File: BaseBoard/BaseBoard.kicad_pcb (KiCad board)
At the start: 4 copper layers, 50 x 35 mm, 59 parts, among them J1 locked, J2 Serial Port, J3 base connector, Q1 PMN48XP, Q2 SSM6L820R, SW1 Battery switch, SW2 boot, SW3 Reset, U1 ESP32-WROOM-E, U3 MCP73831-2ACI-OT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

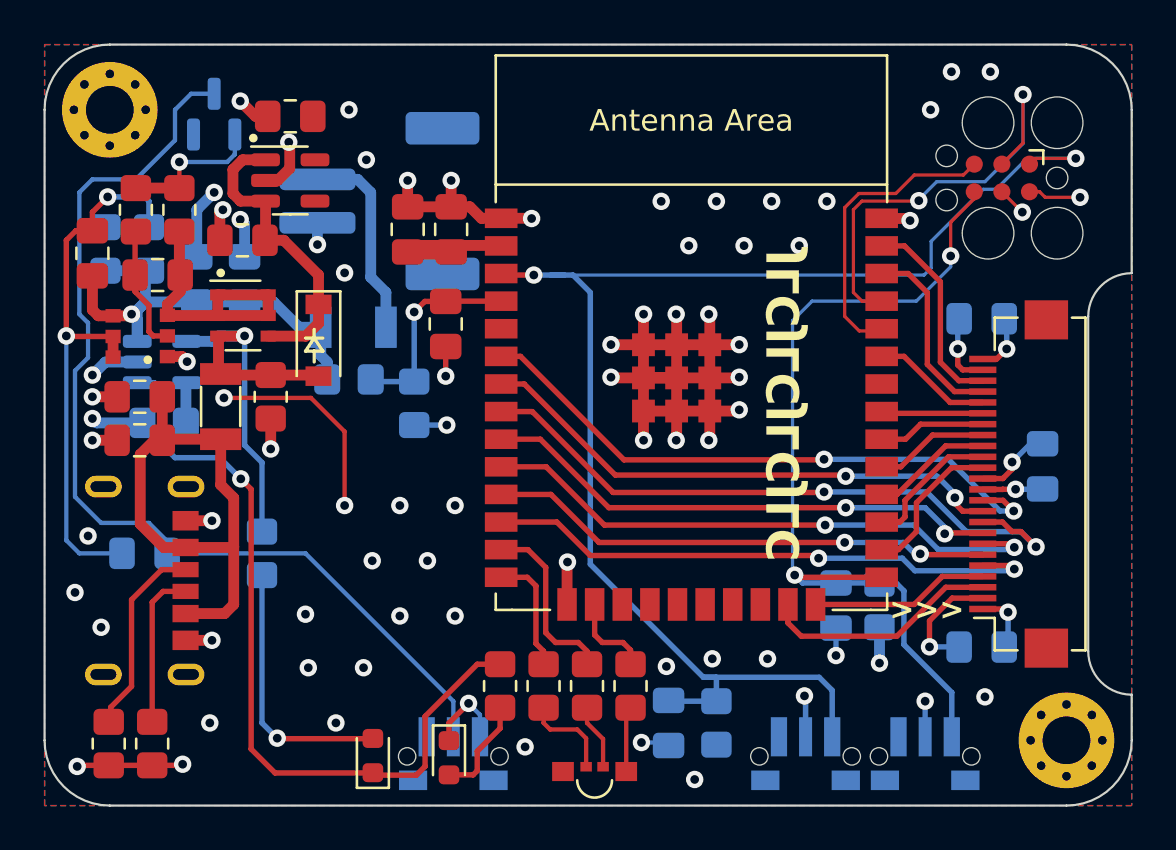
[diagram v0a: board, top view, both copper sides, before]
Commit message: Reorganizes some traces on the BaseBoard
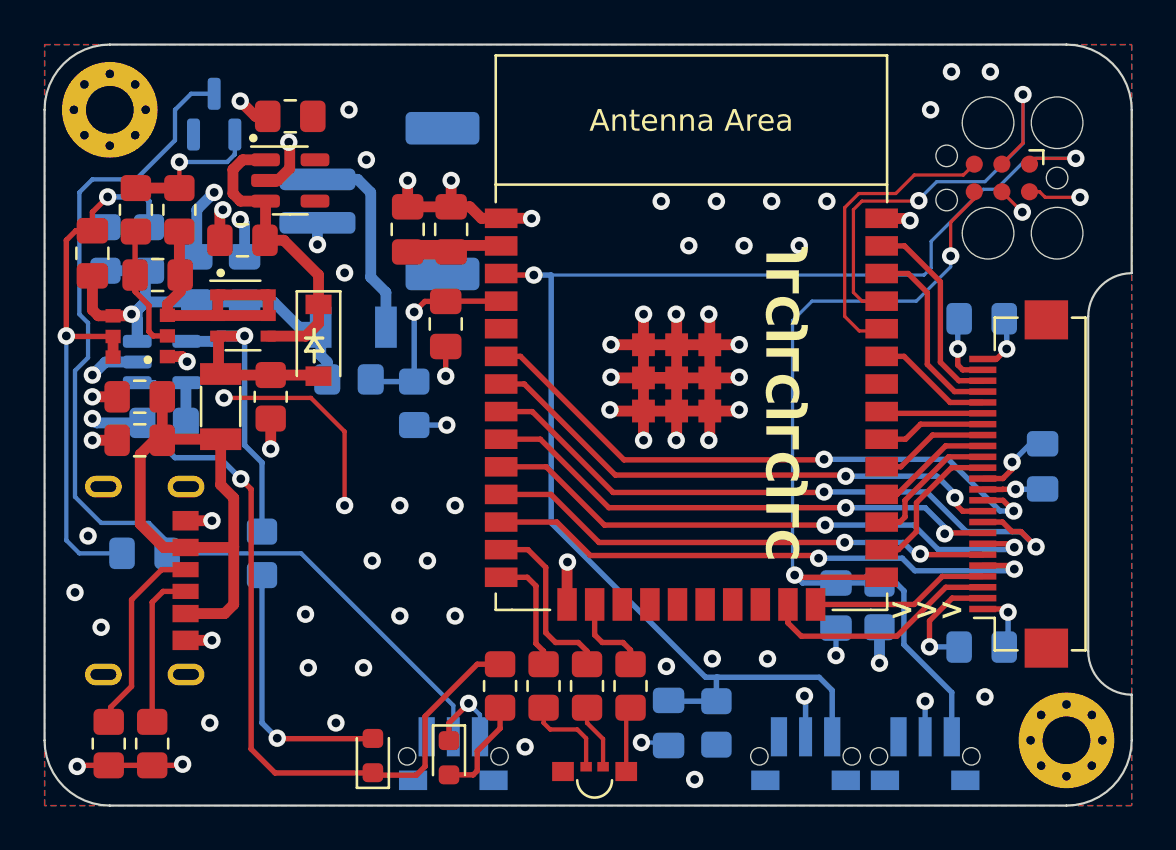
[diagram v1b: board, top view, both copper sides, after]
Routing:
- net ESP_EN: track 66.4 -> 64.7 mm
- net GND: track 100.8 -> 102.3 mm, vias 43 -> 44
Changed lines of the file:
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@@
         (effects (font (size 1 1) (thickness 0.15)))
     )
-    (fp_text value "LED green" (at 0 1.43 90) (layer "F.Fab")
+    (fp_text value "LED green" (at 0 1.43 90) (layer "F.Fab") hide
         (effects (font (size 1 1) (thickness 0.15)))
     )
@@
         (effects (font (size 1 1) (thickness 0.15)))
     )
-    (fp_text value "LED red" (at 0 1.43 90) (layer "F.Fab")
+    (fp_text value "LED red" (at 0 1.43 90) (layer "F.Fab") hide
         (effects (font (size 1 1) (thickness 0.15)))
     )
@@
   (segment (start 149.07 93.805) (end 149.07 96.855) (width 0.5) (layer "F.Cu") (net 2))
   (segment (start 122.95 113.15) (end 121.55 113.15) (width 0.25) (layer "F.Cu") (net 2))
+  (segment (start 146 96.8) (end 146.055 96.855) (width 0.5) (layer "F.Cu") (net 2))
   (segment (start 138.6 111.2) (end 139.5 110.3) (width 0.25) (layer "F.Cu") (net 2))
   (segment (start 150.595 96.855) (end 147.545 96.855) (width 0.5) (layer "F.Cu") (net 2))
@@
   (segment (start 122.2 98.2) (end 123.3375 98.2) (width 0.5) (layer "F.Cu") (net 2))
   (segment (start 158.51 88) (end 158.5 87.99) (width 0.5) (layer "F.Cu") (net 2))
+  (segment (start 146.055 96.855) (end 147.545 96.855) (width 0.5) (layer "F.Cu") (net 2))
   (segment (start 130.1625 86.25) (end 130.722849 86.25) (width 0.5) (layer "F.Cu") (net 2))
   (segment (start 164.074022 99.96) (end 163.15 99.96) (width 0.25) (layer "F.Cu") (net 2))
@@
   (via (at 164.25 94) (size 0.8) (drill 0.4) (layers "F.Cu" "B.Cu") (net 2))
   (via (at 144.05 103.8) (size 0.8) (drill 0.4) (layers "F.Cu" "B.Cu") (net 2))
+  (via (at 146 96.8) (size 0.8) (drill 0.4) (layers "F.Cu" "B.Cu") (net 2))
   (segment (start 137 97.5) (end 138.5 97.5) (width 0.25) (layer "B.Cu") (net 2))
   (segment (start 127 87.6) (end 127 89.7625) (width 0.5) (layer "B.Cu") (net 2))
@@
   (via (at 167.428848 85.235) (size 0.8) (drill 0.4) (layers "F.Cu" "B.Cu") (net 5))
   (via (at 142.5 90.6) (size 0.8) (drill 0.4) (layers "F.Cu" "B.Cu") (net 5))
-  (segment (start 145.1 103.9) (end 145.1 91.4) (width 0.25) (layer "B.Cu") (net 5))
+  (segment (start 143.3 102) (end 143.3 90.6) (width 0.25) (layer "B.Cu") (net 5))
+  (segment (start 151 109.1) (end 150.4 109.1) (width 0.25) (layer "B.Cu") (net 5))
   (segment (start 163.768552 86.655699) (end 165.189251 85.235) (width 0.15) (layer "B.Cu") (net 5))
   (segment (start 160.449251 90.6) (end 160.775 90.274251) (width 0.15) (layer "B.Cu") (net 5))
   (segment (start 143.3 90.6) (end 160.449251 90.6) (width 0.15) (layer "B.Cu") (net 5))
   (segment (start 160.775 89.049251) (end 163.168552 86.655699) (width 0.15) (layer "B.Cu") (net 5))
-  (segment (start 150.3 109.1) (end 150.9 109.1) (width 0.25) (layer "B.Cu") (net 5))
-  (segment (start 156.225 111.8375) (end 156.225 109.7) (width 0.25) (layer "B.Cu") (net 5))
-  (segment (start 143.9 90.6) (end 142.5 90.6) (width 0.25) (layer "B.Cu") (net 5))
   (segment (start 148.7375 110.2) (end 148.7 110.1625) (width 0.25) (layer "B.Cu") (net 5))
+  (segment (start 156.225 111.8375) (end 156.225 109.7) (width 0.25) (layer "B.Cu") (net 5))
   (segment (start 165.189251 85.235) (end 167.428848 85.235) (width 0.15) (layer "B.Cu") (net 5))
+  (segment (start 150.4 109.1) (end 143.3 102) (width 0.25) (layer "B.Cu") (net 5))
   (segment (start 150.9 109.1) (end 150.9 110.2) (width 0.25) (layer "B.Cu") (net 5))
-  (segment (start 156.225 109.7) (end 155.625 109.1) (width 0.25) (layer "B.Cu") (net 5))
-  (segment (start 145.1 91.4) (end 144.3 90.6) (width 0.25) (layer "B.Cu") (net 5))
+  (segment (start 142.5 90.6) (end 143.3 90.6) (width 0.25) (layer "B.Cu") (net 5))
   (segment (start 163.168552 86.655699) (end 163.768552 86.655699) (width 0.15) (layer "B.Cu") (net 5))
   (segment (start 160.775 90.274251) (end 160.775 89.049251) (width 0.15) (layer "B.Cu") (net 5))
+  (segment (start 156.225 109.7) (end 155.625 109.1) (width 0.25) (layer "B.Cu") (net 5))
   (segment (start 150.9 110.2) (end 148.7375 110.2) (width 0.25) (layer "B.Cu") (net 5))
-  (segment (start 155.625 109.1) (end 150.3 109.1) (width 0.25) (layer "B.Cu") (net 5))
-  (segment (start 150.3 109.1) (end 145.1 103.9) (width 0.25) (layer "B.Cu") (net 5))
-  (segment (start 144.3 90.6) (end 143.3 90.6) (width 0.25) (layer "B.Cu") (net 5))
+  (segment (start 155.625 109.1) (end 150.9 109.1) (width 0.25) (layer "B.Cu") (net 5))
   (segment (start 137 92.3) (end 137.4875 91.8125) (width 0.25) (layer "F.Cu") (net 6))
   (segment (start 138.45 91.8125) (end 138.4625 91.8) (width 0.25) (layer "F.Cu") (net 6))
@@
   (segment (start 130.7 111.9) (end 130 111.2) (width 0.25) (layer "B.Cu") (net 49))
   (segment (start 121.6 86.8) (end 122.2 86.2) (width 0.2) (layer "B.Cu") (net 50))
-  (segment (start 138.8 111.8375) (end 138.8 110.2) (width 0.2) (layer "B.Cu") (net 50))
   (segment (start 121.6 88.4) (end 121.6 92.4) (width 0.2) (layer "B.Cu") (net 50))
+  (segment (start 138.8 111.8375) (end 138.8 110.4) (width 0.2) (layer "B.Cu") (net 50))
+  (segment (start 131.8 103.4) (end 125.6375 103.4) (width 0.2) (layer "B.Cu") (net 50))
   (segment (start 122.2 86.2) (end 124.2 86.2) (width 0.2) (layer "B.Cu") (net 50))
-  (segment (start 132 103.4) (end 125.6375 103.4) (width 0.2) (layer "B.Cu") (net 50))
-  (segment (start 138.8 110.2) (end 132 103.4) (width 0.2) (layer "B.Cu") (net 50))
   (segment (start 121.6 88.4) (end 121.6 86.8) (width 0.2) (layer "B.Cu") (net 50))
   (segment (start 124.8 102) (end 125.6375 102.8375) (width 0.2) (layer "B.Cu") (net 50))
@@
   (segment (start 122.8 88.4) (end 121.6 88.4) (width 0.2) (layer "B.Cu") (net 50))
   (segment (start 122.6 102) (end 124.8 102) (width 0.2) (layer "B.Cu") (net 50))
+  (segment (start 138.8 110.4) (end 131.8 103.4) (width 0.2) (layer "B.Cu") (net 50))
   (segment (start 126 83) (end 126.7375 82.2625) (width 0.2) (layer "B.Cu") (net 50))
   (segment (start 126 84.4) (end 126 83) (width 0.2) (layer "B.Cu") (net 50))

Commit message: Adds label for on/off button
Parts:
- added kibuzzard-63029C06: G***, kibuzzard-63029C06, B.Cu at (138.8, 109.8)
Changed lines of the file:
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@@
-(kicad_pcb (version 20220331) (generator pcbnew)
+(kicad_pcb (version 20220818) (generator pcbnew)
   (general
     (thickness 1.6)
@@
       (connect_pads (clearance 0))
       (min_thickness 0.254) (filled_areas_thickness no)
-      (keepout (tracks allowed) (vias not_allowed) (pads allowed ) (copperpour not_allowed) (footprints not_allowed))
+      (keepout (tracks allowed) (vias not_allowed) (pads allowed) (copperpour not_allowed) (footprints not_allowed))
       (fill (thermal_gap 0.508) (thermal_bridge_width 0.508))
       (polygon
@@
       (thermal_bridge_angle 45))
   )
+  (footprint "kibuzzard-63029C06" (layer "B.Cu")
+    (at 138.8 109.75 180)
+    (descr "Generated with KiBuzzard")
+    (tags "kb_params=eyJBbGlnbm1lbnRDaG9pY2UiOiAiQ2VudGVyIiwgIkNhcExlZnRDaG9pY2UiOiAiWyIsICJDYXBSaWdodENob2ljZSI6ICJdIiwgIkZvbnRDb21ib0JveCI6ICJVYnVudHVNb25vLUIiLCAiSGVpZ2h0Q3RybCI6ICIxIiwgIkxheWVyQ29tYm9Cb3giOiAiRi5TaWxrUyIsICJNdWx0aUxpbmVUZXh0IjogIm9uL29mZiIsICJQYWRkaW5nQm90dG9tQ3RybCI6ICI1IiwgIlBhZGRpbmdMZWZ0Q3RybCI6ICI1IiwgIlBhZGRpbmdSaWdodEN0cmwiOiAiNSIsICJQYWRkaW5nVG9wQ3RybCI6ICI1IiwgIldpZHRoQ3RybCI6ICIifQ==")
+    (attr board_only exclude_from_pos_files exclude_from_bom)
+    (fp_text reference "kibuzzard-63029C06" (at 0 4.064529) (layer "B.SilkS") hide
+        (effects (font (size 0 0)) (justify mirror))
+    )
+    (fp_text value "G***" (at 0 -4.064529) (layer "B.SilkS") hide
+        (effects (font (size 0 0)) (justify mirror))
+    )
+    (fp_poly
+      (pts
+        (xy -2.153444 -0.0508)
+        (xy -2.144514 -0.141288)
+        (xy -2.117725 -0.212725)
+        (xy -2.071092 -0.259159)
+        (xy -2.002631 -0.274638)
+        (xy -1.935758 -0.259159)
+        (xy -1.887537 -0.212725)
+        (xy -1.858367 -0.141288)
+        (xy -1.848644 -0.0508)
+        (xy -1.857573 0.039489)
+        (xy -1.884362 0.110331)
+        (xy -1.930995 0.15617)
+        (xy -1.999456 0.17145)
+        (xy -2.06633 0.15617)
+        (xy -2.11455 0.110331)
+        (xy -2.14372 0.039489)
+        (xy -2.153444 -0.0508)
+      )
+      (stroke (width 0) (type solid)) (fill solid) (layer "B.SilkS"))
+    (fp_poly
+      (pts
+        (xy 0.227806 -0.0508)
+        (xy 0.236736 -0.141288)
+        (xy 0.263525 -0.212725)
+        (xy 0.310158 -0.259159)
+        (xy 0.378619 -0.274638)
+        (xy 0.445492 -0.259159)
+        (xy 0.493713 -0.212725)
+        (xy 0.522883 -0.141288)
+        (xy 0.532606 -0.0508)
+        (xy 0.523677 0.039489)
+        (xy 0.496888 0.110331)
+        (xy 0.450255 0.15617)
+        (xy 0.381794 0.17145)
+        (xy 0.31492 0.15617)
+        (xy 0.2667 0.110331)
+        (xy 0.23753 0.039489)
+        (xy 0.227806 -0.0508)
+      )
+      (stroke (width 0) (type solid)) (fill solid) (layer "B.SilkS"))
+    (fp_poly
+      (pts
+        (xy -2.351881 1.016529)
+        (xy -2.68261 1.016529)
+        (xy -2.68261 -1.016529)
+        (xy -2.351881 -1.016529)
+        (xy -1.999456 -1.016529)
+        (xy -1.999456 -0.4445)
+        (xy -2.075061 -0.437356)
+        (xy -2.143125 -0.415925)
+        (xy -2.203053 -0.381397)
+        (xy -2.25425 -0.334963)
+        (xy -2.295723 -0.277614)
+        (xy -2.326481 -0.210344)
+        (xy -2.345531 -0.133945)
+        (xy -2.351881 -0.049212)
+        (xy -2.345333 0.03433)
+        (xy -2.325688 0.110331)
+        (xy -2.294334 0.177403)
+        (xy -2.252663 0.234156)
+        (xy -2.201267 0.279797)
+        (xy -2.140744 0.313531)
+        (xy -2.072878 0.334367)
+        (xy -1.999456 0.341312)
+        (xy -1.925042 0.334367)
+        (xy -1.857375 0.313531)
+        (xy -1.797447 0.279797)
+        (xy -1.74625 0.234156)
+        (xy -1.704777 0.177403)
+        (xy -1.674019 0.110331)
+        (xy -1.654969 0.03433)
+        (xy -1.648619 -0.049212)
+        (xy -1.654969 -0.133945)
+        (xy -1.674019 -0.210344)
+        (xy -1.704578 -0.277614)
+        (xy -1.745456 -0.334963)
+        (xy -1.796058 -0.381397)
+        (xy -1.855788 -0.415925)
+        (xy -1.923852 -0.437356)
+        (xy -1.999456 -0.4445)
+        (xy -1.999456 -1.016529)
+        (xy -0.904081 -1.016529)
+        (xy -0.904081 -0.423863)
+        (xy -1.099344 -0.423863)
+        (xy -1.099344 -0.028575)
+        (xy -1.105297 0.061516)
+        (xy -1.123156 0.122237)
+        (xy -1.219994 0.168275)
+        (xy -1.26365 0.166687)
+        (xy -1.308894 0.161925)
+        (xy -1.308894 -0.423863)
+        (xy -1.504156 -0.423863)
+        (xy -1.504156 0.29845)
+        (xy -1.445617 0.312341)
+        (xy -1.374775 0.325437)
+        (xy -1.294408 0.334962)
+        (xy -1.207294 0.338137)
+        (xy -1.125934 0.331986)
+        (xy -1.059656 0.313531)
+        (xy -0.966787 0.243681)
+        (xy -0.918369 0.135731)
+        (xy -0.907653 0.069652)
+        (xy -0.904081 -0.003175)
+        (xy -0.904081 -0.423863)
+        (xy -0.904081 -1.016529)
+        (xy -0.532606 -1.016529)
+        (xy -0.532606 -0.6858)
+        (xy -0.735806 -0.6858)
+        (xy -0.291306 0.6858)
+        (xy -0.091281 0.6858)
+        (xy -0.532606 -0.6858)
+        (xy -0.532606 -1.016529)
+        (xy 0.381794 -1.016529)
+        (xy 0.381794 -0.4445)
+        (xy 0.306189 -0.437356)
+        (xy 0.238125 -0.415925)
+        (xy 0.178197 -0.381397)
+        (xy 0.127 -0.334963)
+        (xy 0.085527 -0.277614)
+        (xy 0.054769 -0.210344)
+        (xy 0.035719 -0.133945)
+        (xy 0.029369 -0.049212)
+        (xy 0.035917 0.03433)
+        (xy 0.055563 0.110331)
+        (xy 0.086916 0.177403)
+        (xy 0.128588 0.234156)
+        (xy 0.179983 0.279797)
+        (xy 0.240506 0.313531)
+        (xy 0.308372 0.334367)
+        (xy 0.381794 0.341312)
+        (xy 0.456208 0.334367)
+        (xy 0.523875 0.313531)
+        (xy 0.583803 0.279797)
+        (xy 0.635 0.234156)
+        (xy 0.676473 0.177403)
+        (xy 0.707231 0.110331)
+        (xy 0.726281 0.03433)
+        (xy 0.732631 -0.049212)
+        (xy 0.726281 -0.133945)
+        (xy 0.707231 -0.210344)
+        (xy 0.676672 -0.277614)
+        (xy 0.635794 -0.334963)
+        (xy 0.585192 -0.381397)
+        (xy 0.525463 -0.415925)
+        (xy 0.457398 -0.437356)
+        (xy 0.381794 -0.4445)
+        (xy 0.381794 -1.016529)
+        (xy 0.997744 -1.016529)
+        (xy 0.997744 -0.423863)
+        (xy 0.997744 0.160337)
+        (xy 0.834231 0.160337)
+        (xy 0.834231 0.322262)
+        (xy 0.997744 0.322262)
+        (xy 0.997744 0.365125)
+        (xy 1.004292 0.447873)
+        (xy 1.023938 0.515144)
+        (xy 1.094581 0.610394)
+        (xy 1.196181 0.661194)
+        (xy 1.313656 0.676275)
+        (xy 1.440656 0.665162)
+        (xy 1.558131 0.62865)
+        (xy 1.524794 0.4699)
+        (xy 1.433513 0.496094)
+        (xy 1.329531 0.509588)
+        (xy 1.277938 0.504825)
+        (xy 1.235075 0.484187)
+        (xy 1.205706 0.438944)
+        (xy 1.194594 0.36195)
+        (xy 1.194594 0.322262)
+        (xy 1.500981 0.322262)
+        (xy 1.500981 0.160337)
+        (xy 1.194594 0.160337)
+        (xy 1.194594 -0.423863)
+        (xy 0.997744 -0.423863)
+        (xy 0.997744 -1.016529)
+        (xy 1.791494 -1.016529)
+        (xy 1.791494 -0.423863)
+        (xy 1.791494 0.160337)
+        (xy 1.627981 0.160337)
+        (xy 1.627981 0.322262)
+        (xy 1.791494 0.322262)
+        (xy 1.791494 0.365125)
+        (xy 1.798042 0.447873)
+        (xy 1.817688 0.515144)
+        (xy 1.888331 0.610394)
+        (xy 1.989931 0.661194)
+        (xy 2.107406 0.676275)
+        (xy 2.234406 0.665162)
+        (xy 2.351881 0.62865)
+        (xy 2.318544 0.4699)
+        (xy 2.227263 0.496094)
+        (xy 2.123281 0.509588)
+        (xy 2.071688 0.504825)
+        (xy 2.028825 0.484187)
+        (xy 1.999456 0.438944)
+        (xy 1.988344 0.36195)
+        (xy 1.988344 0.322262)
+        (xy 2.294731 0.322262)
+        (xy 2.294731 0.160337)
+        (xy 1.988344 0.160337)
+        (xy 1.988344 -0.423863)
+        (xy 1.791494 -0.423863)
+        (xy 1.791494 -1.016529)
+        (xy 2.351881 -1.016529)
+        (xy 2.68261 -1.016529)
+        (xy 2.68261 1.016529)
+        (xy 2.351881 1.016529)
+        (xy -2.351881 1.016529)
+      )
+      (stroke (width 0) (type solid)) (fill solid) (layer "B.SilkS"))
+  )
   (footprint "Package_TO_SOT_SMD:SOT-23" (layer "B.Cu")
     (at 127.8 83.2 90)
@@
     (connect_pads (clearance 0))
     (min_thickness 0.254) (filled_areas_thickness no)
-    (keepout (tracks not_allowed) (vias not_allowed) (pads not_allowed ) (copperpour not_allowed) (footprints allowed))
+    (keepout (tracks not_allowed) (vias not_allowed) (pads not_allowed) (copperpour not_allowed) (footprints allowed))
     (fill (thermal_gap 0.508) (thermal_bridge_width 0.508) (island_removal_mode 2) (island_area_min 10))
     (polygon

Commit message: Update version label on PCBs to 1.0
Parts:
- removed kibuzzard-62829F6C: G***, kibuzzard-62829F6C
- added kibuzzard-63029CBF: G***, kibuzzard-63029CBF, B.Cu at (131.6, 113.4)

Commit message: Small adjustment to the height of the on/off label
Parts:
- moved kibuzzard-63029C06 0.15 mm to (138.8, 109.6)
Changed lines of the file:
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@@
     (attr board_only exclude_from_pos_files exclude_from_bom)
     (fp_text reference "kibuzzard-63029CBF" (at 0 3.891492) (layer "B.SilkS") hide
-        (effects (font (size 0 0)) (justify mirror))
+        (effects (font (size 0 0) (thickness 0.15)) (justify mirror))
     )
     (fp_text value "G***" (at 0 -3.891492) (layer "B.SilkS") hide
-        (effects (font (size 0 0)) (justify mirror))
+        (effects (font (size 0 0) (thickness 0.15)) (justify mirror))
     )
     (fp_poly
@@
   )
   (footprint "kibuzzard-63029C06" (layer "B.Cu")
-    (at 138.8 109.75 180)
+    (at 138.8 109.6 180)
     (descr "Generated with KiBuzzard")
     (tags "kb_params=eyJBbGlnbm1lbnRDaG9pY2UiOiAiQ2VudGVyIiwgIkNhcExlZnRDaG9pY2UiOiAiWyIsICJDYXBSaWdodENob2ljZSI6ICJdIiwgIkZvbnRDb21ib0JveCI6ICJVYnVudHVNb25vLUIiLCAiSGVpZ2h0Q3RybCI6ICIxIiwgIkxheWVyQ29tYm9Cb3giOiAiRi5TaWxrUyIsICJNdWx0aUxpbmVUZXh0IjogIm9uL29mZiIsICJQYWRkaW5nQm90dG9tQ3RybCI6ICI1IiwgIlBhZGRpbmdMZWZ0Q3RybCI6ICI1IiwgIlBhZGRpbmdSaWdodEN0cmwiOiAiNSIsICJQYWRkaW5nVG9wQ3RybCI6ICI1IiwgIldpZHRoQ3RybCI6ICIifQ==")
     (attr board_only exclude_from_pos_files exclude_from_bom)
     (fp_text reference "kibuzzard-63029C06" (at 0 4.064529) (layer "B.SilkS") hide
-        (effects (font (size 0 0)) (justify mirror))
+        (effects (font (size 0 0) (thickness 0.15)) (justify mirror))
     )
     (fp_text value "G***" (at 0 -4.064529) (layer "B.SilkS") hide
-        (effects (font (size 0 0)) (justify mirror))
+        (effects (font (size 0 0) (thickness 0.15)) (justify mirror))
     )
     (fp_poly
